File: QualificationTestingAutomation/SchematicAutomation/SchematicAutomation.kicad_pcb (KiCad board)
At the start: 4 copper layers, 242.6 x 165.1 mm, 268 parts, among them IC1 TUSB2046B, J1 OBD Connector, J10 OBD Connector, J11 OBD Connector, J12 0015912120, J13 Barrel_Jack_MountingPin, J14 Banana Jack, J15 Banana Jack, J16 12401610E4_2A, J17 Banana Jack, J18 OBD Connector, J19 OBD Connector, J2 OBD Connector, J20 OBD Connector, J21 OBD Connector, J22 OBD Connector, J3 OBD Connector, J4 OBD Connector, J5 OBD Connector, J6 OBD Connector, J7 OBD Connector, J8 OBD Connector, J9 OBD Connector, Q1 ULN2003ADR, Q10 2N7002DW, Q11 2N7002DW, Q12 2N7002DW, Q13 2N7002DW, Q14 2N7002DW, Q15 2N7002DW, Q16 2N7002DW, Q17 2N7002DW, Q18 2N7002DW, Q19 2N7002DW, Q2 ULN2003ADR, Q20 2N7002DW, Q21 2N7002DW, Q22 2N7002DW, Q23 2N7002DW, Q24 2N7002DW, Q25 2N7002DW, Q26 2N7002DW, Q27 2N7002DW, Q28 2N7002DW, Q29 2N7002DW, Q3 2N7002DW, Q30 2N7002DW, Q35 2N7002DW, Q36 2N7002DW, Q37 2N7002DW, Q38 2N7002DW, Q4 2N7002DW, Q5 2N7002DW, Q6 2N7002DW, Q7 2N7002DW, Q8 2N7002DW, Q9 2N7002DW, U1 DG408LE, U10 MAX14752, U11 MAX14752, U12 MAX14752, U13 MAX14752, U14 FT4232HL-REEL, U15 FT4232HL-REEL, U16 DG408LE, U17 DS18B20_, U18 FT4232HL-REEL, U19 CD74HC4067SM96, U2 DG408LE, U20 CD4070B, U21 CD4070B, U22 CD4070B, U23 CD4070B, U24 CD4070B, U25 CD4070B, U26 CD4070B, U28 CD4070B, U3 AT90USB1287-AU, U30 MAX324CUA, U31 MAX324CUA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

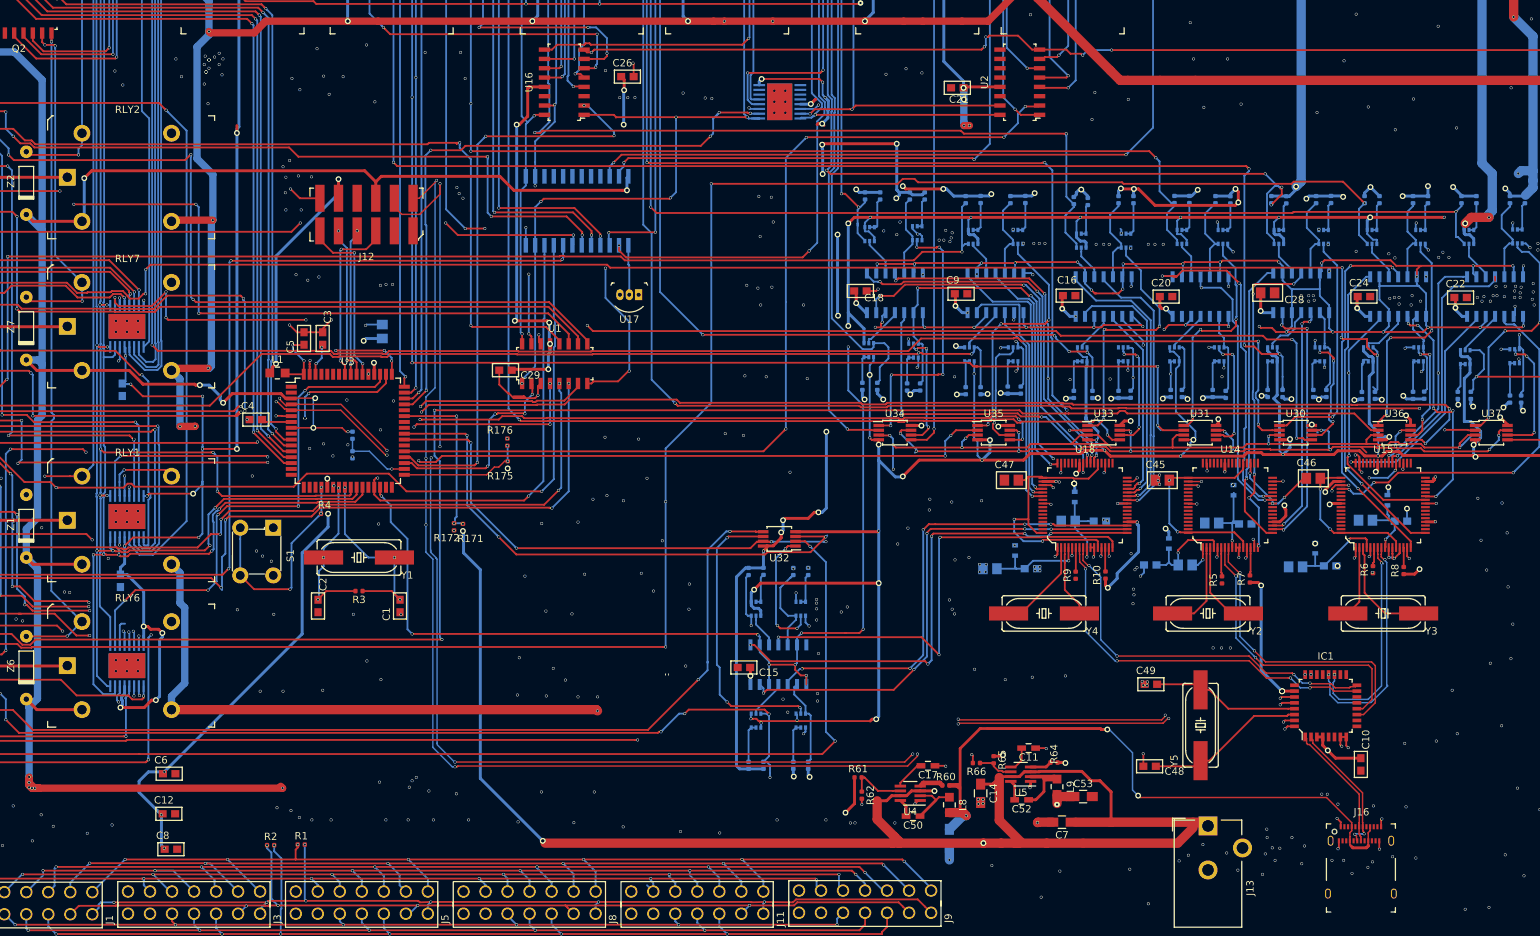
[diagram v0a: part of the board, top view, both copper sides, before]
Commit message: added schematic symbols
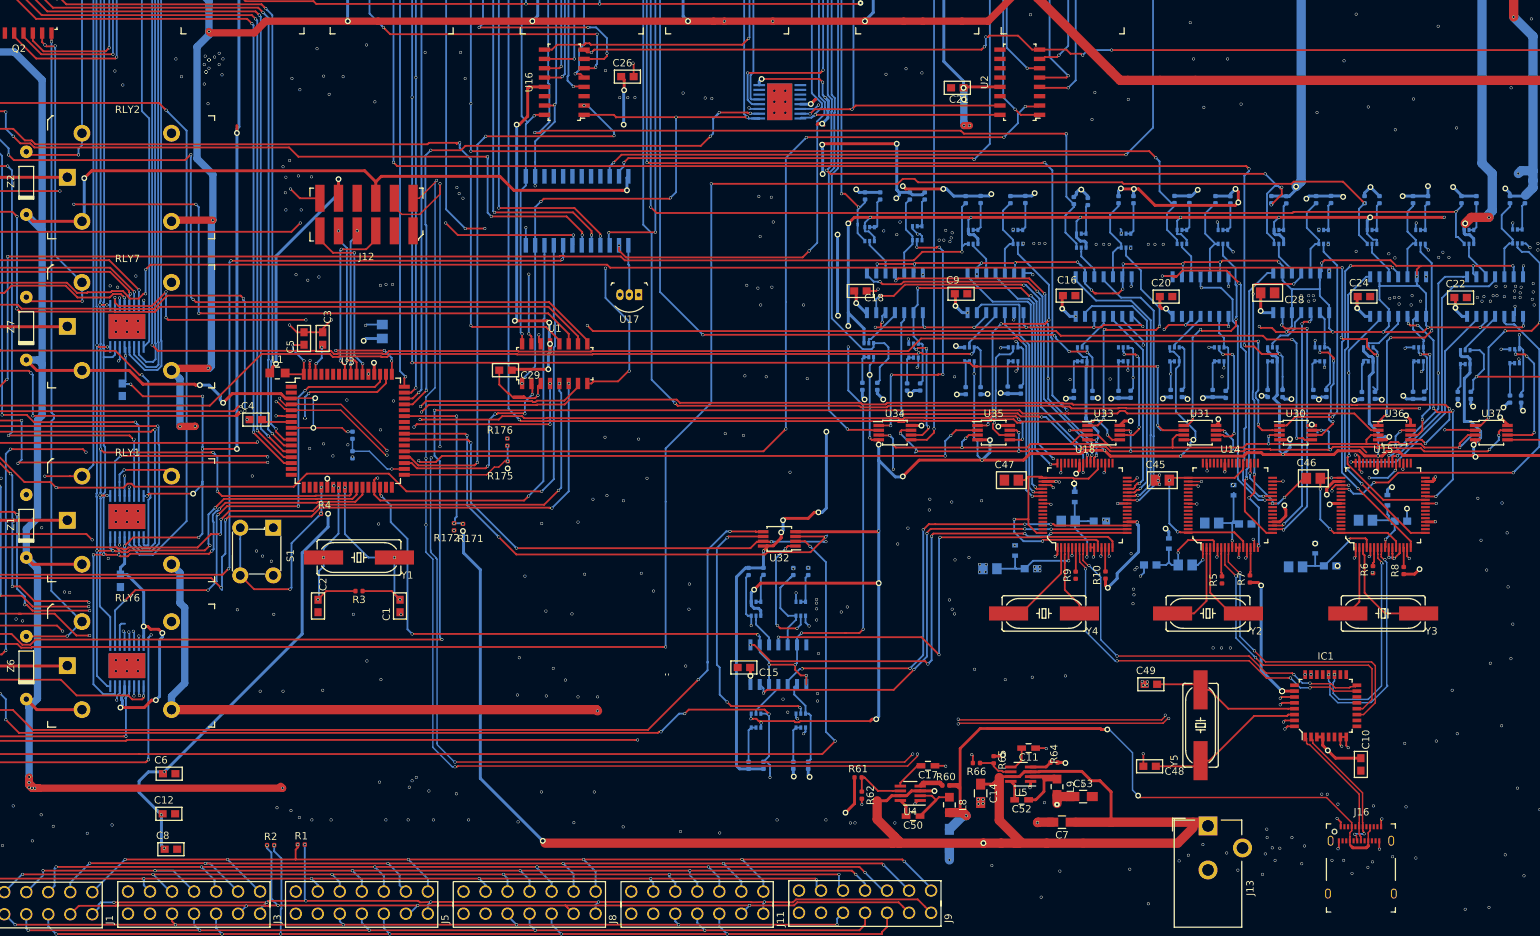
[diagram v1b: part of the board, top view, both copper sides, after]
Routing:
- net GND: track 202.4 -> 205.9 mm, vias 573 -> 575
- net Net-(C46-Pad2): track 34.0 -> 32.5 mm, vias 4 -> 5
- net 1_J1850+: track 127.4 -> 126.1 mm
- net +3V3: track 413.0 -> 413.6 mm
- net /RS232/sheet5BDC5154/Tx_3V3: track 34.9 -> 34.3 mm
- net VAA: vias 43 -> 45
- net 1_GarminRX: vias 4 -> 3

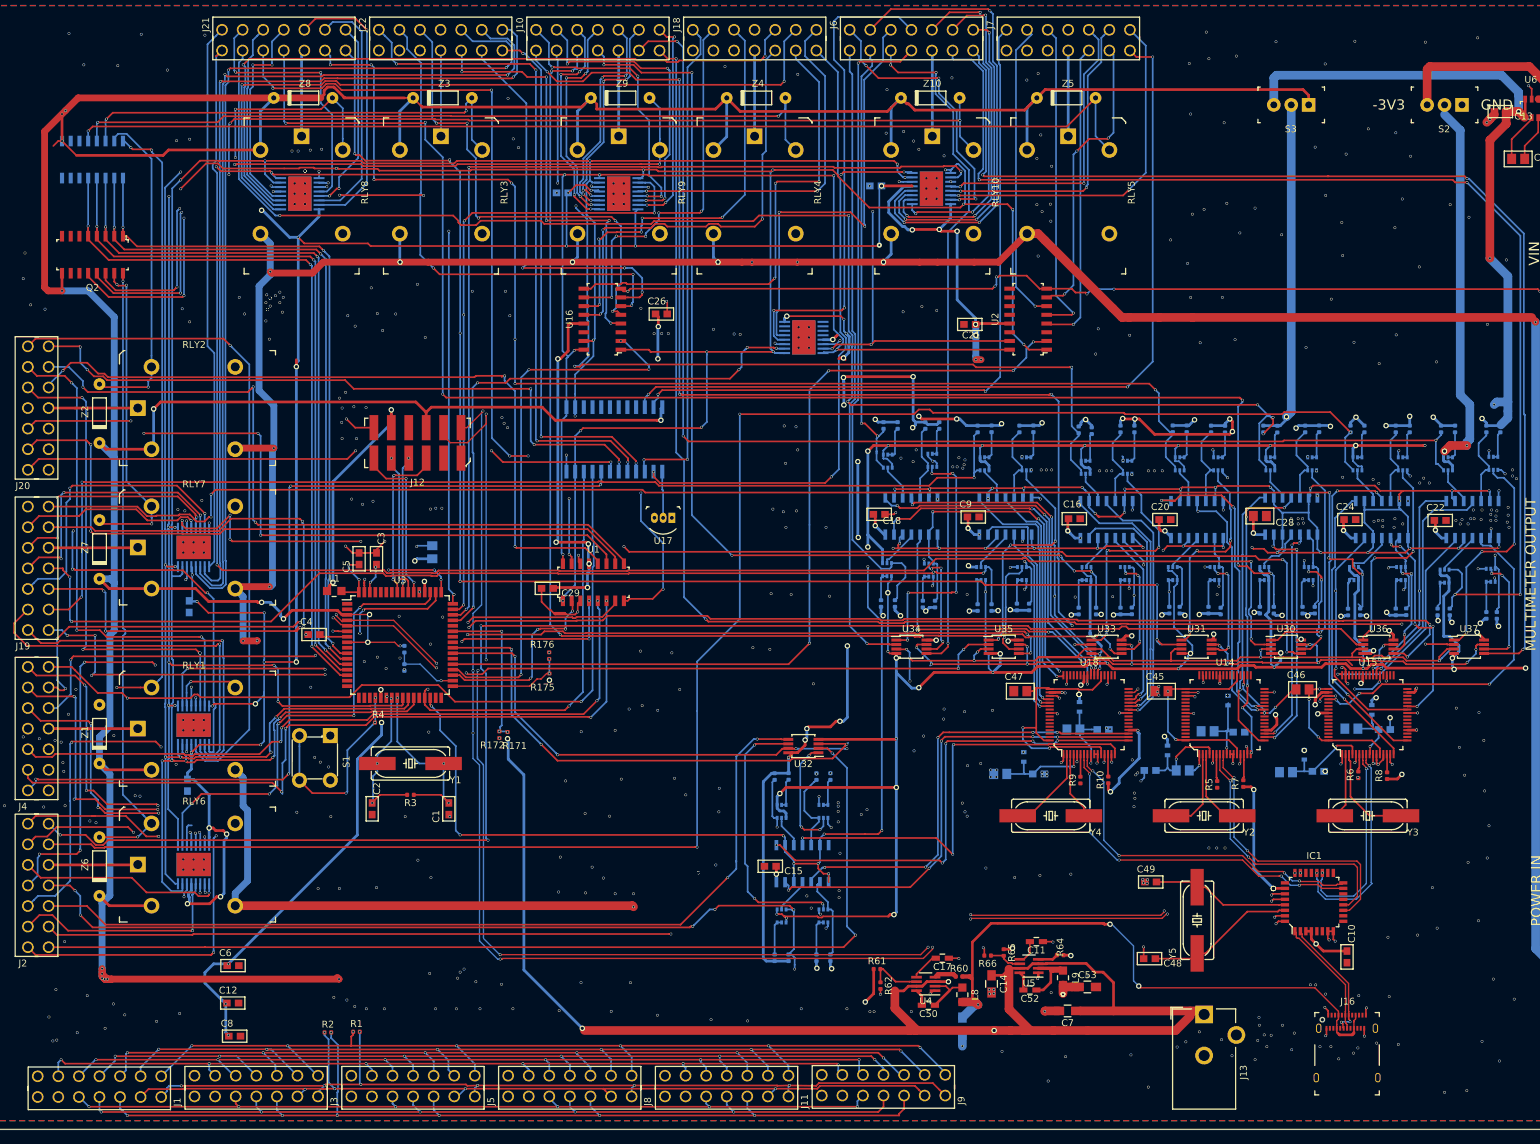
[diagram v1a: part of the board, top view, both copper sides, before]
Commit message: Started the coding and some clean up of the pcb
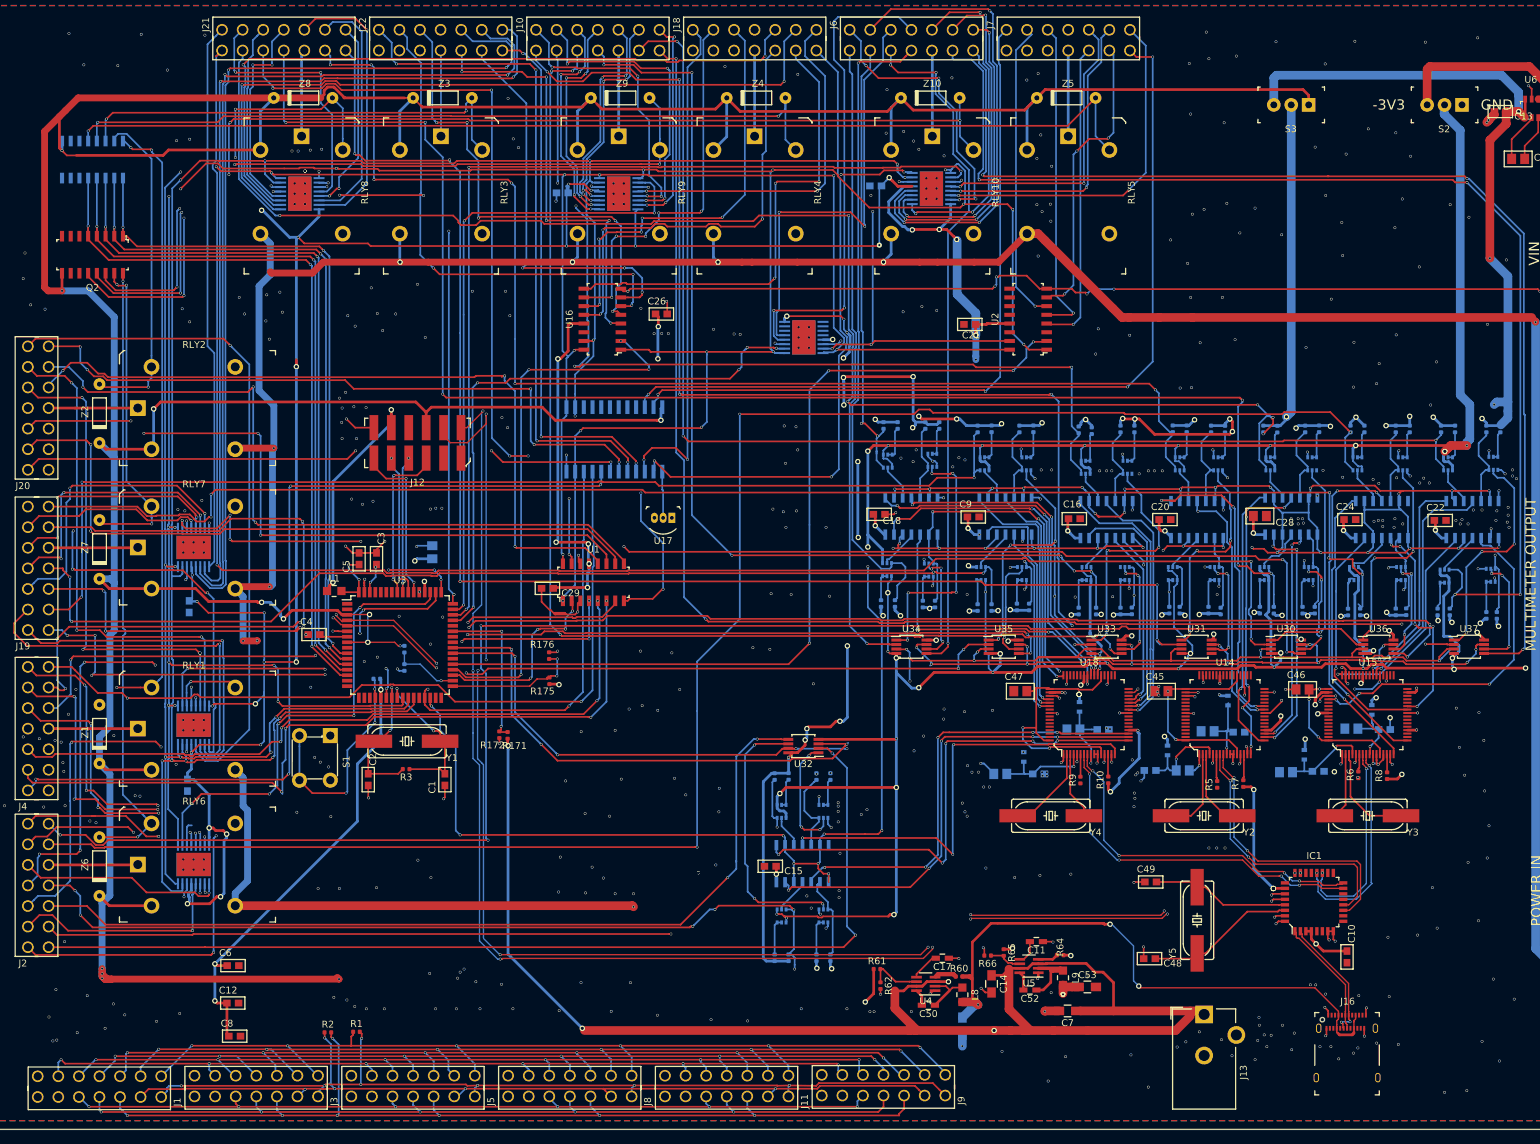
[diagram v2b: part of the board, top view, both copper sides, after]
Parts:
- R4: moved to B.Cu
- moved R4 6.37 mm to (94.3, 117.2)
- moved C1 4.29 mm to (104.2, 131.9)
- moved C2 4.29 mm to (93.0, 131.9)
- moved R3 3.80 mm to (98.6, 130.4)
- moved Y1 3.28 mm to (98.7, 126.3)
- moved R175 0.57 mm to (119.4, 117.5)
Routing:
- net VAA: track 680.7 -> 638.2 mm, vias 45 -> 43
- net GND: track 205.9 -> 226.2 mm, vias 575 -> 549
- net +3V3: track 413.6 -> 423.7 mm, vias 84 -> 79
- net Net-(R4-Pad1): track 29.8 -> 34.0 mm
- net Net-(C1-Pad2): track 26.1 -> 22.5 mm, vias 3 -> 2
- net Net-(R175-Pad2): track 17.0 -> 19.8 mm
- net 4_OWB_MAIN: track 72.0 -> 73.8 mm
- net /RS232/sheet5BC04BA5/RX_3V3: track 70.1 -> 71.3 mm
- net 4_OWB_SEC: track 92.2 -> 93.3 mm
- net TX_CONT: track 198.9 -> 197.8 mm
- net Net-(C2-Pad1): track 22.2 -> 21.2 mm, vias 3 -> 2
- net -VSW: track 521.1 -> 520.3 mm, vias 36 -> 35
- net +5V: track 817.1 -> 817.5 mm, vias 21 -> 17
- net RS232INV: track 400.1 -> 400.2 mm, vias 42 -> 41
- net /RS232/sheet5BD54784/RTS_3V3: vias 2 -> 1
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
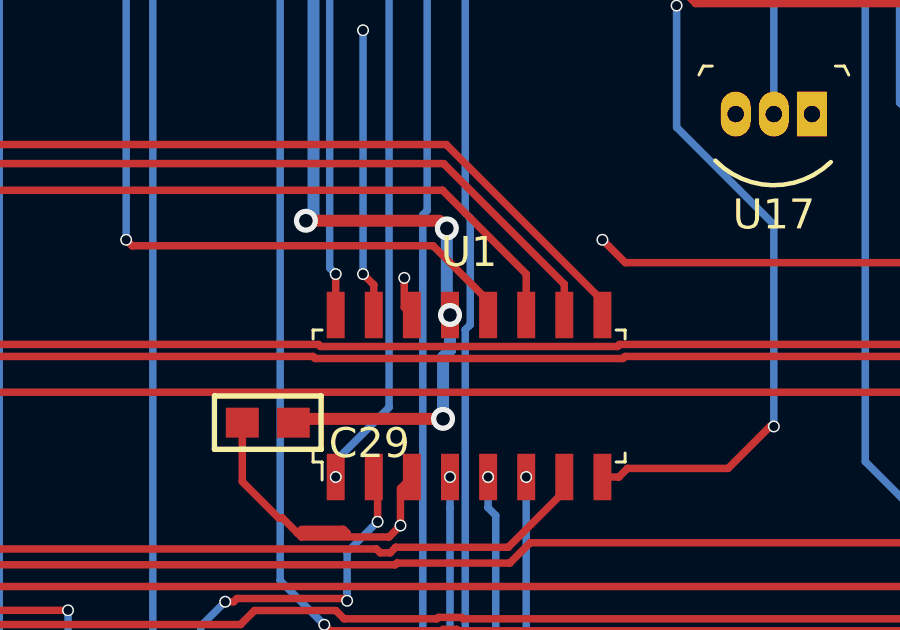
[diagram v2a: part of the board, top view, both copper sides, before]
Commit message: RX TX mixup was solved by changing RX_3V3 and TX_3V3 on the XOR side Same goes for CTS and RTS and some general clean up
Signed-off-by: Riyad Alalami <riyadhelalami@gmail.com>
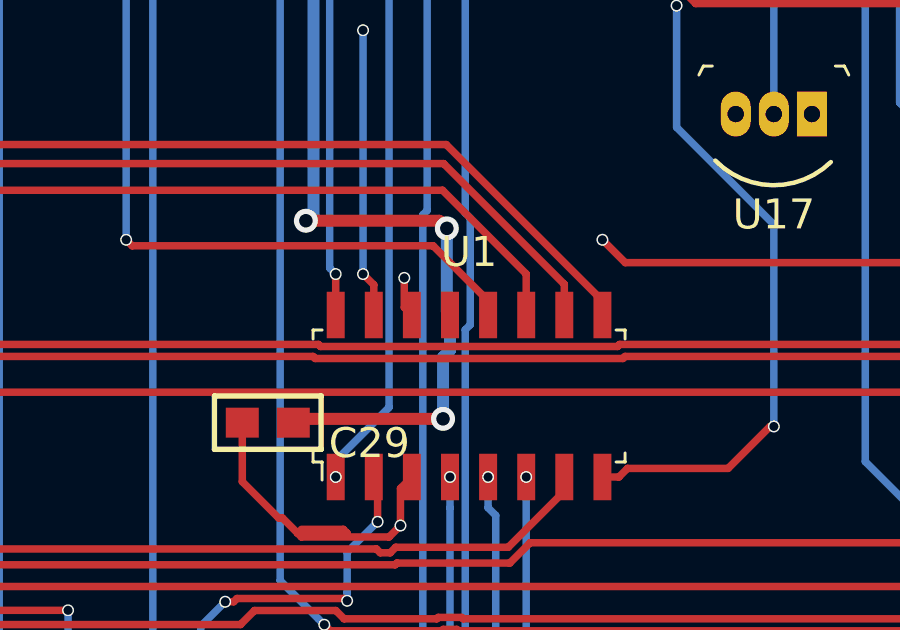
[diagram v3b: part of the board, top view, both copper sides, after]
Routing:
- net VAA: vias 43 -> 42
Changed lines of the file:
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@@
-(kicad_pcb (version 20171130) (host pcbnew 5.0.0)
+(kicad_pcb (version 20171130) (host pcbnew "(5.0.0)")
   (general
     (thickness 1.6)
     (drawings 9)
-    (tracks 7989)
+    (tracks 7988)
     (zones 0)
     (modules 268)
@@
     (solder_mask_min_width 0.1)
     (aux_axis_origin 0 0)
-    (visible_elements FFF9FFFF)
+    (visible_elements 7FFFFFFF)
     (pcbplotparams
       (layerselection 0x010fc_ffffffff)
@@
   (segment (start 121.031 70.5485) (end 120.672232 70.5485) (width 0.4) (layer F.Cu) (net 22))
   (segment (start 120.672232 70.5485) (end 82.677 70.5485) (width 1.27) (layer In1.Cu) (net 22))
-  (segment (start 120.672232 70.5485) (end 120.672232 97.155) (width 0.4) (layer B.Cu) (net 22))
-  (via (at 120.418232 97.282) (size 0.8) (drill 0.45) (layers F.Cu B.Cu) (net 22))
-  (segment (start 120.672232 97.155) (end 120.545232 97.282) (width 0.4) (layer B.Cu) (net 22))
-  (segment (start 120.545232 97.282) (end 120.418232 97.282) (width 0.4) (layer B.Cu) (net 22))
-  (via (at 125.117232 97.536) (size 0.8) (drill 0.45) (layers F.Cu B.Cu) (net 22))
-  (segment (start 124.863232 97.282) (end 125.117232 97.536) (width 0.4) (layer F.Cu) (net 22))
-  (segment (start 120.418232 97.282) (end 124.863232 97.282) (width 0.4) (layer F.Cu) (net 22))
-  (segment (start 125.117232 97.536) (end 125.117232 100.319232) (width 0.4) (layer B.Cu) (net 22))
-  (segment (start 125.117232 100.319232) (end 125.222 100.424) (width 0.4) (layer B.Cu) (net 22))
-  (via (at 125.222 100.424) (size 0.8) (drill 0.45) (layers F.Cu B.Cu) (net 22))
-  (segment (start 125.222 101.599) (end 124.990232 101.830768) (width 0.4) (layer B.Cu) (net 22))
-  (segment (start 125.222 100.424) (end 125.222 101.599) (width 0.4) (layer B.Cu) (net 22))
-  (via (at 124.990232 103.886) (size 0.8) (drill 0.45) (layers F.Cu B.Cu) (net 22))
-  (segment (start 124.990232 101.830768) (end 124.990232 103.886) (width 0.4) (layer B.Cu) (net 22))
-  (segment (start 120.125232 103.886) (end 119.998232 104.013) (width 0.4) (layer F.Cu) (net 22))
-  (segment (start 124.990232 103.886) (end 120.125232 103.886) (width 0.4) (layer F.Cu) (net 22))
   (segment (start 85.858 49.800232) (end 85.858 48.757) (width 0.4) (layer B.Cu) (net 22))
   (segment (start 82.826232 52.832) (end 85.858 49.800232) (width 0.4) (layer B.Cu) (net 22))
@@
   (segment (start 178.8795 53.2765) (end 178.8795 61.1505) (width 1.27) (layer B.Cu) (net 22))
   (segment (start 178.8795 61.1505) (end 181.61 63.881) (width 1.27) (layer B.Cu) (net 22))
+  (via (at 124.990232 103.886) (size 0.8) (drill 0.45) (layers F.Cu B.Cu) (net 22) (status 1000000))
+  (via (at 120.418232 97.282) (size 0.8) (drill 0.45) (layers F.Cu B.Cu) (net 22) (status 1000000))
+  (via (at 125.117232 97.536) (size 0.8) (drill 0.45) (layers F.Cu B.Cu) (net 22) (status 1000000))
+  (segment (start 125.117232 100.319232) (end 125.222 100.424) (width 0.4) (layer B.Cu) (net 22) (status 1000000))
+  (segment (start 124.863232 97.282) (end 125.117232 97.536) (width 0.4) (layer F.Cu) (net 22) (status 1000000))
+  (segment (start 124.990232 101.830768) (end 124.990232 103.886) (width 0.4) (layer B.Cu) (net 22) (status 1000000))
+  (segment (start 125.117232 97.536) (end 125.117232 100.319232) (width 0.4) (layer B.Cu) (net 22) (status 1000000))
+  (segment (start 120.545232 97.282) (end 120.418232 97.282) (width 0.4) (layer B.Cu) (net 22) (status 1000000))
+  (segment (start 120.125232 103.886) (end 119.998232 104.013) (width 0.4) (layer F.Cu) (net 22) (status 1000000))
+  (segment (start 120.418232 97.282) (end 124.863232 97.282) (width 0.4) (layer F.Cu) (net 22) (status 1000000))
+  (segment (start 120.672232 70.5485) (end 120.672232 97.155) (width 0.4) (layer B.Cu) (net 22) (status 1000000))
+  (segment (start 124.990232 103.886) (end 120.125232 103.886) (width 0.4) (layer F.Cu) (net 22) (status 1000000))
+  (segment (start 125.222 101.599) (end 124.990232 101.830768) (width 0.4) (layer B.Cu) (net 22) (status 1000000))
+  (segment (start 125.222 100.424) (end 125.222 101.599) (width 0.4) (layer B.Cu) (net 22) (status 1000000))
+  (segment (start 120.672232 97.155) (end 120.545232 97.282) (width 0.4) (layer B.Cu) (net 22) (status 1000000))
   (via (at 80.137 122.936) (size 0.4) (drill 0.3) (layers F.Cu B.Cu) (net 27))
   (via (at 79.121 128.651) (size 0.4) (drill 0.3) (layers F.Cu B.Cu) (net 27))
